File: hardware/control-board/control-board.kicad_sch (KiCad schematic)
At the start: 2 parts

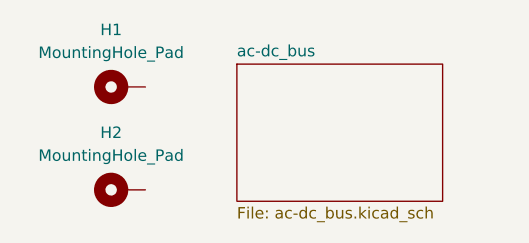
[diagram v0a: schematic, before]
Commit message: added soft start and bleeder resistor to dc bus
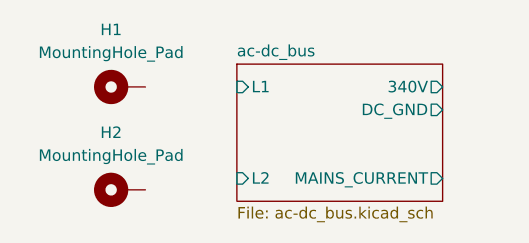
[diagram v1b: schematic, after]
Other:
- sheet ac-dc_bus ports: added 340V, DC_GND, L1, L2, MAINS_CURRENT; removed none
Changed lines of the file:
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@@
+			)
+		)
+		(pin "MAINS_CURRENT" output
+			(at 71.12 50.8 0)
+			(effects
+				(font
+					(size 1.27 1.27)
+				)
+				(justify right)
+			)
+		)
+		(pin "L1" input
+			(at 48.26 40.64 180)
+			(effects
+				(font
+					(size 1.27 1.27)
+				)
+				(justify left)
+			)
+		)
+		(pin "L2" input
+			(at 48.26 50.8 180)
+			(effects
+				(font
+					(size 1.27 1.27)
+				)
+				(justify left)
+			)
+		)
+		(pin "340V" output
+			(at 71.12 40.64 0)
+			(effects
+				(font
+					(size 1.27 1.27)
+				)
+				(justify right)
+			)
+		)
+		(pin "DC_GND" output
+			(at 71.12 43.18 0)
+			(effects
+				(font
+					(size 1.27 1.27)
+				)
+				(justify right)
 			)
 		)

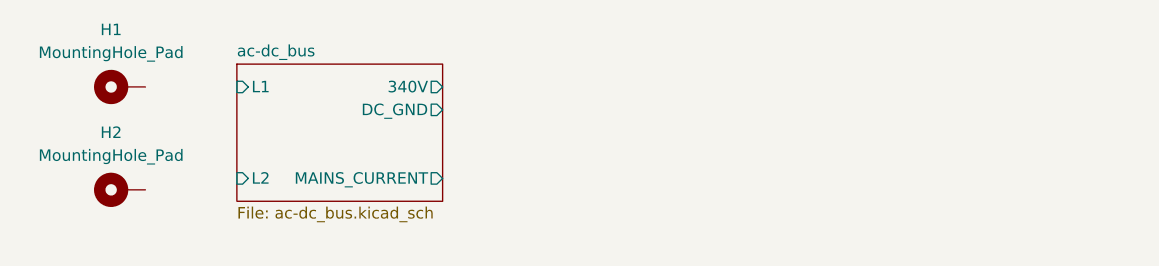
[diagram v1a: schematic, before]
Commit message: added voltage divider and start work on inverter and tank circuits
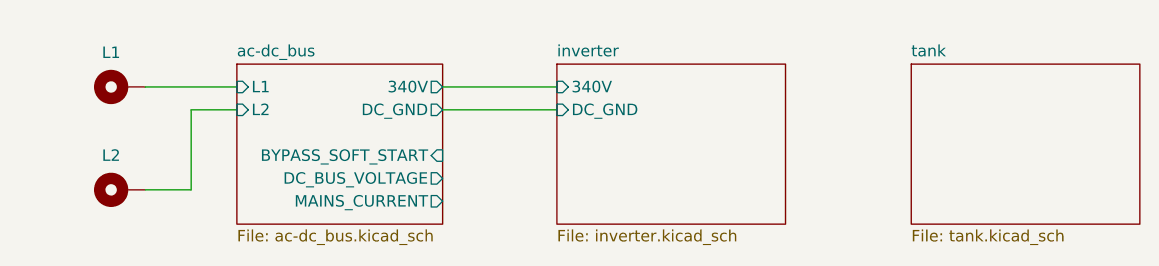
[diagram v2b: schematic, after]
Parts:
- renumbered H1 to L1, H2 to L2
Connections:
- net ac-dc_bus/L1: now also L1.1
- net ac-dc_bus/L2: now also L2.1
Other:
- added sheet inverter (inverter.kicad_sch)
- added sheet tank (tank.kicad_sch)
- sheet ac-dc_bus ports: added BYPASS_SOFT_START, DC_BUS_VOLTAGE; removed none
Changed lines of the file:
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@@
 	(generator_version "9.0")
 	(paper "A4")
+	(wire
+		(pts
+			(xy 38.1 40.64) (xy 48.26 40.64)
+		)
+		(stroke
+			(width 0)
+			(type default)
+		)
+	)
+	(wire
+		(pts
+			(xy 71.12 43.18) (xy 83.82 43.18)
+		)
+		(stroke
+			(width 0)
+			(type default)
+		)
+	)
+	(wire
+		(pts
+			(xy 71.12 40.64) (xy 83.82 40.64)
+		)
+		(stroke
+			(width 0)
+			(type default)
+		)
+	)
+	(wire
+		(pts
+			(xy 43.18 52.07) (xy 43.18 43.18)
+		)
+		(stroke
+			(width 0)
+			(type default)
+		)
+	)
+	(wire
+		(pts
+			(xy 43.18 43.18) (xy 48.26 43.18)
+		)
+		(stroke
+			(width 0)
+			(type default)
+		)
+	)
+	(wire
+		(pts
+			(xy 38.1 52.07) (xy 43.18 52.07)
+		)
+		(stroke
+			(width 0)
+			(type default)
+		)
+	)
 	(symbol
 		(lib_id "Mechanical:MountingHole_Pad")
@@
 		(dnp no)
 		(fields_autoplaced yes)
-		(property "Reference" "H1"
-			(at 34.29 34.29 90)
+		(property "Reference" "L1"
+			(at 34.29 36.83 90)
 			(effects
 				(font
@@
 					(size 1.27 1.27)
 				)
+				(hide yes)
 			)
 		)
@@
 			(project ""
 				(path "/19f0fb17-7370-4e5d-b0c6-f8a287a0a6cc"
-					(reference "H1")
+					(reference "L1")
 					(unit 1)
 				)
@@
 		(dnp no)
 		(fields_autoplaced yes)
-		(property "Reference" "H2"
-			(at 34.29 45.72 90)
+		(property "Reference" "L2"
+			(at 34.29 48.26 90)
 			(effects
 				(font
@@
 					(size 1.27 1.27)
 				)
+				(hide yes)
 			)
 		)
@@
 			(project ""
 				(path "/19f0fb17-7370-4e5d-b0c6-f8a287a0a6cc"
-					(reference "H2")
+					(reference "L2")
 					(unit 1)
+				)
+			)
+		)
+	)
+	(sheet
+		(at 83.82 38.1)
+		(size 25.4 17.78)
+		(exclude_from_sim no)
+		(in_bom yes)
+		(on_board yes)
+		(dnp no)
+		(fields_autoplaced yes)
+		(stroke
+			(width 0.1524)
+			(type solid)
+		)
+		(fill
+			(color 0 0 0 0.0000)
+		)
+		(property "Sheetname" "inverter"
+			(at 83.82 37.3884 0)
+			(effects
+				(font
+					(size 1.27 1.27)
+				)
+				(justify left bottom)
+			)
+		)
+		(property "Sheetfile" "inverter.kicad_sch"
+			(at 83.82 56.4646 0)
+			(effects
+				(font
+					(size 1.27 1.27)
+				)
+				(justify left top)
+			)
+		)
+		(pin "340V" input
+			(at 83.82 40.64 180)
+			(effects
+				(font
+					(size 1.27 1.27)
+				)
+				(justify left)
+			)
+		)
+		(pin "DC_GND" input
+			(at 83.82 43.18 180)
+			(effects
+				(font
+					(size 1.27 1.27)
+				)
+				(justify left)
+			)
+		)
+		(instances
+			(project "control-board"
+				(path "/19f0fb17-7370-4e5d-b0c6-f8a287a0a6cc"
+					(page "3")
+				)
+			)
+		)
+	)
+	(sheet
+		(at 123.19 38.1)
+		(size 25.4 17.78)
+		(exclude_from_sim no)
+		(in_bom yes)
+		(on_board yes)
+		(dnp no)
+		(fields_autoplaced yes)
+		(stroke
+			(width 0.1524)
+			(type solid)
+		)
+		(fill
+			(color 0 0 0 0.0000)
+		)
+		(property "Sheetname" "tank"
+			(at 123.19 37.3884 0)
+			(effects
+				(font
+					(size 1.27 1.27)
+				)
+				(justify left bottom)
+			)
+		)
+		(property "Sheetfile" "tank.kicad_sch"
+			(at 123.19 56.4646 0)
+			(effects
+				(font
+					(size 1.27 1.27)
+				)
+				(justify left top)
+			)
+		)
+		(instances
+			(project "control-board"
+				(path "/19f0fb17-7370-4e5d-b0c6-f8a287a0a6cc"
+					(page "4")
 				)
 			)
@@
 	(sheet
 		(at 48.26 38.1)
-		(size 22.86 15.24)
+		(size 22.86 17.78)
 		(exclude_from_sim no)
 		(in_bom yes)
@@
 		)
 		(property "Sheetfile" "ac-dc_bus.kicad_sch"
-			(at 48.26 53.9246 0)
+			(at 48.26 56.4646 0)
 			(effects
 				(font
@@
 		)
 		(pin "MAINS_CURRENT" output
-			(at 71.12 50.8 0)
+			(at 71.12 53.34 0)
 			(effects
 				(font
@@
 		)
 		(pin "L2" input
-			(at 48.26 50.8 180)
+			(at 48.26 43.18 180)
 			(effects
 				(font
@@
 			(effects
 				(font
+					(size 1.27 1.27)
+				)
+				(justify right)
+			)
+		)
+		(pin "BYPASS_SOFT_START" input
+			(at 71.12 48.26 0)
+			(effects
+				(font
+					(size 1.27 1.27)
+				)
+				(justify right)
+			)
+		)
+		(pin "DC_BUS_VOLTAGE" output
+			(at 71.12 50.8 0)
+			(effects
+				(font

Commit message: final draft of ac-dc done
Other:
- sheet ac-dc_bus ports: added DC_BUS_VOLTAGE_VALID; removed none
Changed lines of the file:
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@@
-	(wire
-		(pts
-			(xy 71.12 43.18) (xy 83.82 43.18)
-		)
-		(stroke
-			(width 0)
-			(type default)
-		)
-	)
-	(wire
-		(pts
-			(xy 71.12 40.64) (xy 83.82 40.64)
-		)
-		(stroke
-			(width 0)
-			(type default)
-		)
-	)
 	(wire
 		(pts
@@
 	)
 	(sheet
-		(at 83.82 38.1)
-		(size 25.4 17.78)
+		(at 92.71 38.1)
+		(size 25.4 20.32)
 		(exclude_from_sim no)
 		(in_bom yes)
@@
 		)
 		(property "Sheetname" "inverter"
-			(at 83.82 37.3884 0)
+			(at 92.71 37.3884 0)
 			(effects
 				(font
@@
 		)
 		(property "Sheetfile" "inverter.kicad_sch"
-			(at 83.82 56.4646 0)
+			(at 92.71 59.0046 0)
 			(effects
 				(font
@@
 		)
 		(pin "340V" input
-			(at 83.82 40.64 180)
+			(at 92.71 40.64 180)
 			(effects
 				(font
@@
 		)
 		(pin "DC_GND" input
-			(at 83.82 43.18 180)
+			(at 92.71 43.18 180)
 			(effects
 				(font
@@
 	(sheet
 		(at 123.19 38.1)
-		(size 25.4 17.78)
+		(size 25.4 20.32)
 		(exclude_from_sim no)
 		(in_bom yes)
@@
 		)
 		(property "Sheetfile" "tank.kicad_sch"
-			(at 123.19 56.4646 0)
+			(at 123.19 59.0046 0)
 			(effects
 				(font
@@
 	(sheet
 		(at 48.26 38.1)
-		(size 22.86 17.78)
+		(size 33.02 20.32)
 		(exclude_from_sim no)
 		(in_bom yes)
@@
 		)
 		(property "Sheetfile" "ac-dc_bus.kicad_sch"
-			(at 48.26 56.4646 0)
+			(at 48.26 59.0046 0)
 			(effects
 				(font
@@
 		)
 		(pin "MAINS_CURRENT" output
-			(at 71.12 53.34 0)
+			(at 81.28 55.88 0)
 			(effects
 				(font
@@
 		)
 		(pin "340V" output
-			(at 71.12 40.64 0)
+			(at 81.28 40.64 0)
 			(effects
 				(font
@@
 		)
 		(pin "DC_GND" output
-			(at 71.12 43.18 0)
+			(at 81.28 43.18 0)
 			(effects
 				(font
@@
 		)
 		(pin "BYPASS_SOFT_START" input
-			(at 71.12 48.26 0)
+			(at 81.28 50.8 0)
 			(effects
 				(font
@@
 		)
 		(pin "DC_BUS_VOLTAGE" output
-			(at 71.12 50.8 0)
-			(effects
-				(font
+			(at 81.28 53.34 0)
+			(effects
+				(font
+					(size 1.27 1.27)
+				)
+				(justify right)
+			)
+		)
+		(pin "DC_BUS_VOLTAGE_VALID" output
+			(at 81.28 48.26 0)
+			(effects
+				(font

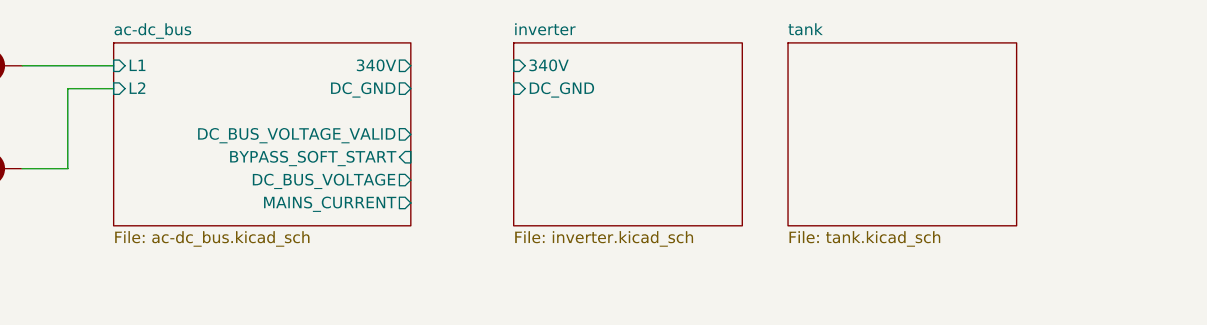
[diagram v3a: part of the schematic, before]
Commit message: reasearch, added section and finished negative bias addition to intervet side a
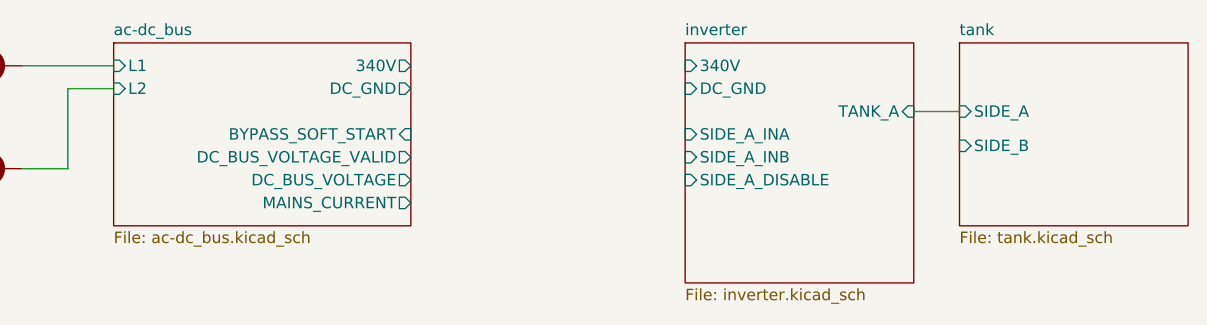
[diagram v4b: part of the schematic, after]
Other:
- sheet inverter ports: added SIDE_A_DISABLE, SIDE_A_INA, SIDE_A_INB, TANK_A; removed none
- sheet tank ports: added SIDE_A, SIDE_B; removed none
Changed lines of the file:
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@@
+		)
+	)
+	(wire
+		(pts
+			(xy 137.16 45.72) (xy 142.24 45.72)
+		)
+		(stroke
+			(width 0)
+			(type default)
 		)
 	)
@@
 	)
 	(sheet
-		(at 92.71 38.1)
-		(size 25.4 20.32)
+		(at 111.76 38.1)
+		(size 25.4 26.67)
 		(exclude_from_sim no)
 		(in_bom yes)
@@
 		)
 		(property "Sheetname" "inverter"
-			(at 92.71 37.3884 0)
+			(at 111.76 37.3884 0)
 			(effects
 				(font
@@
 		)
 		(property "Sheetfile" "inverter.kicad_sch"
-			(at 92.71 59.0046 0)
+			(at 111.76 65.3546 0)
 			(effects
 				(font
@@
 		)
 		(pin "340V" input
-			(at 92.71 40.64 180)
+			(at 111.76 40.64 180)
 			(effects
 				(font
@@
 		)
 		(pin "DC_GND" input
-			(at 92.71 43.18 180)
+			(at 111.76 43.18 180)
+			(effects
+				(font
+					(size 1.27 1.27)
+				)
+				(justify left)
+			)
+		)
+		(pin "TANK_A" input
+			(at 137.16 45.72 0)
+			(effects
+				(font
+					(size 1.27 1.27)
+				)
+				(justify right)
+			)
+		)
+		(pin "SIDE_A_INA" input
+			(at 111.76 48.26 180)
+			(effects
+				(font
+					(size 1.27 1.27)
+				)
+				(justify left)
+			)
+		)
+		(pin "SIDE_A_INB" input
+			(at 111.76 50.8 180)
+			(effects
+				(font
+					(size 1.27 1.27)
+				)
+				(justify left)
+			)
+		)
+		(pin "SIDE_A_DISABLE" input
+			(at 111.76 53.34 180)
 			(effects
 				(font
@@
 	)
 	(sheet
-		(at 123.19 38.1)
+		(at 142.24 38.1)
 		(size 25.4 20.32)
 		(exclude_from_sim no)
@@
 		)
 		(property "Sheetname" "tank"
-			(at 123.19 37.3884 0)
+			(at 142.24 37.3884 0)
 			(effects
 				(font
@@
 		)
 		(property "Sheetfile" "tank.kicad_sch"
-			(at 123.19 59.0046 0)
+			(at 142.24 59.0046 0)
 			(effects
 				(font
@@
 				)
 				(justify left top)
+			)
+		)
+		(pin "SIDE_B" input
+			(at 142.24 49.53 180)
+			(effects
+				(font
+					(size 1.27 1.27)
+				)
+				(justify left)
+			)
+		)
+		(pin "SIDE_A" input
+			(at 142.24 45.72 180)
+			(effects
+				(font
+					(size 1.27 1.27)
+				)
+				(justify left)
 			)
 		)
@@
 		)
 		(pin "BYPASS_SOFT_START" input
-			(at 81.28 50.8 0)
+			(at 81.28 48.26 0)
 			(effects
 				(font
@@
 		)
 		(pin "DC_BUS_VOLTAGE_VALID" output
-			(at 81.28 48.26 0)
-			(effects
-				(font
+			(at 81.28 50.8 0)
+			(effects
+				(font

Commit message: mirrored side a inverter to side b
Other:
- sheet inverter ports: added SIDE_B_DISABLE, SIDE_B_INA, SIDE_B_INB, TANK_B; removed none
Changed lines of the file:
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@@
+	(wire
+		(pts
+			(xy 137.16 49.53) (xy 142.24 49.53)
+		)
+		(stroke
+			(width 0)
+			(type default)
+		)
+	)
 	(wire
 		(pts
@@
 			(effects
 				(font
+					(size 1.27 1.27)
+				)
+				(justify left)
+			)
+		)
+		(pin "TANK_B" input
+			(at 137.16 49.53 0)
+			(effects
+				(font
+					(size 1.27 1.27)
+				)
+				(justify right)
+			)
+		)
+		(pin "SIDE_B_INA" input
+			(at 111.76 57.15 180)
+			(effects
+				(font
+					(size 1.27 1.27)
+				)
+				(justify left)
+			)
+		)
+		(pin "SIDE_B_INB" input
+			(at 111.76 59.69 180)
+			(effects
+				(font
+					(size 1.27 1.27)
+				)
+				(justify left)
+			)
+		)
+		(pin "SIDE_B_DISABLE" input
+			(at 111.76 62.23 180)
+			(effects
+				(font

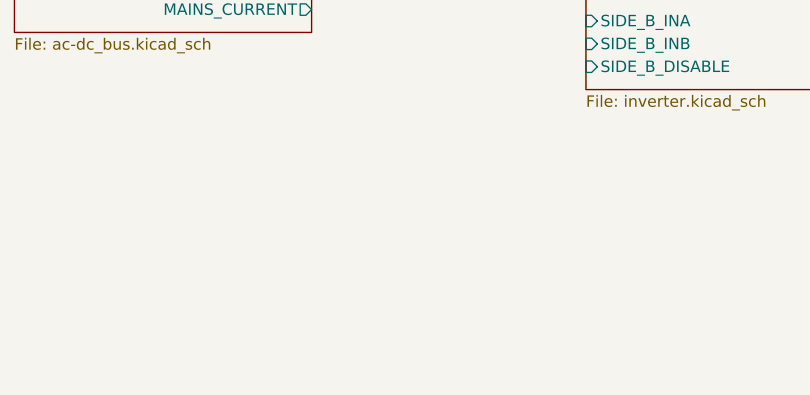
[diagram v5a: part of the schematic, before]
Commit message: started mcu schematic
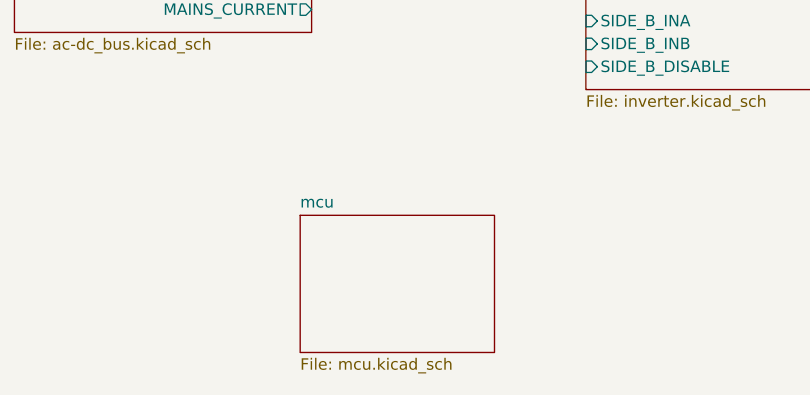
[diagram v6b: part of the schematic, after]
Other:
- added sheet mcu (mcu.kicad_sch)
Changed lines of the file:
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@@
+	)
+	(sheet
+		(at 80.01 78.74)
+		(size 21.59 15.24)
+		(exclude_from_sim no)
+		(in_bom yes)
+		(on_board yes)
+		(dnp no)
+		(fields_autoplaced yes)
+		(stroke
+			(width 0.1524)
+			(type solid)
+		)
+		(fill
+			(color 0 0 0 0.0000)
+		)
+		(property "Sheetname" "mcu"
+			(at 80.01 78.0284 0)
+			(effects
+				(font
+					(size 1.27 1.27)
+				)
+				(justify left bottom)
+			)
+		)
+		(property "Sheetfile" "mcu.kicad_sch"
+			(at 80.01 94.5646 0)
+			(effects
+				(font
+					(size 1.27 1.27)
+				)
+				(justify left top)
+			)
+		)
+		(instances
+			(project "control-board"
+				(path "/19f0fb17-7370-4e5d-b0c6-f8a287a0a6cc"
+					(page "5")
+				)
+			)
+		)
 	)
 	(sheet

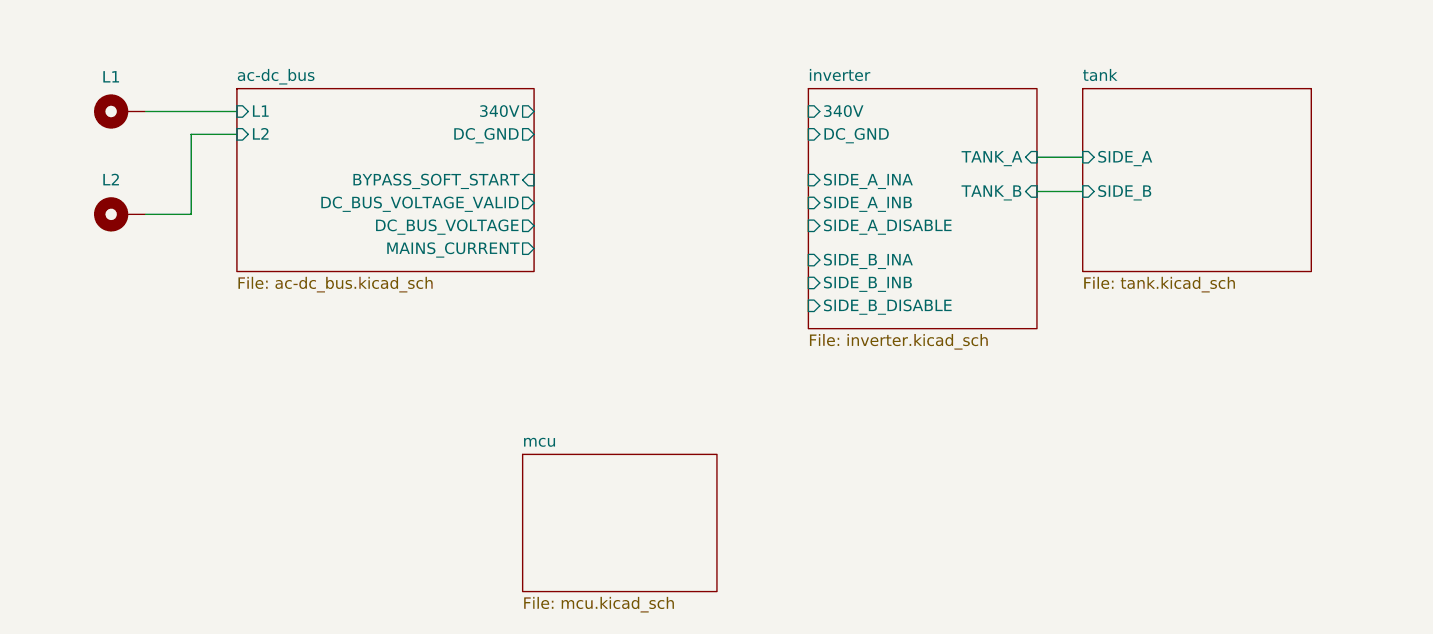
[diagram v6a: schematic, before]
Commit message: mcu controller added
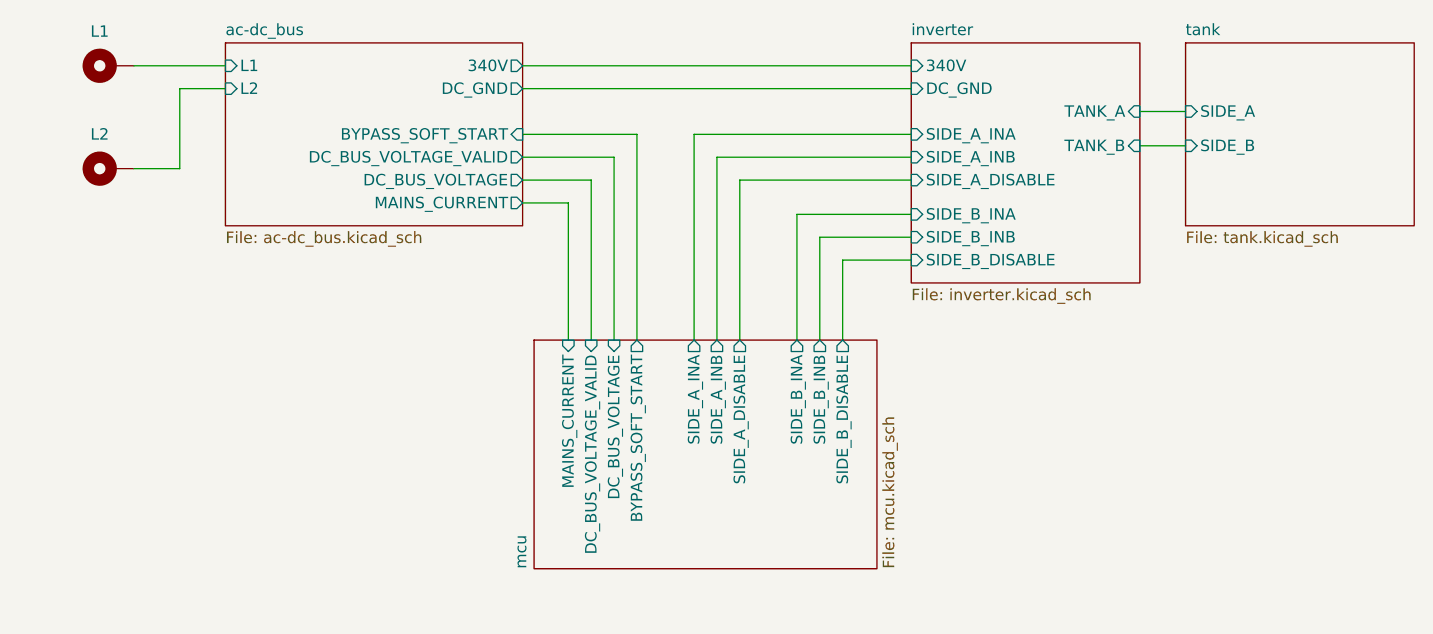
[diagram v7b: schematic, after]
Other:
- sheet mcu ports: added BYPASS_SOFT_START, DC_BUS_VOLTAGE, DC_BUS_VOLTAGE_VALID, MAINS_CURRENT, SIDE_A_DISABLE, SIDE_A_INA, SIDE_A_INB, SIDE_B_DISABLE, SIDE_B_INA, SIDE_B_INB; removed none
- moved on the sheet: L1, L2
